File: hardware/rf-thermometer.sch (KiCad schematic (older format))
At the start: 2 parts

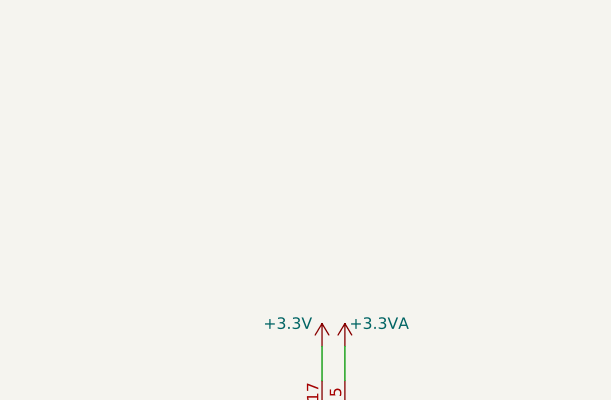
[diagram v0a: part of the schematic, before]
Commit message: Add power bypassing capacitors + filtering inductor for ADC
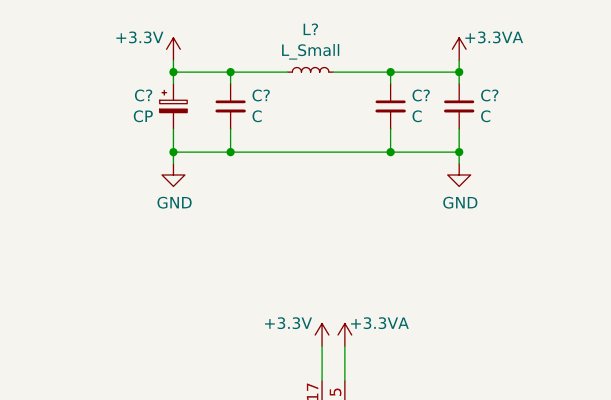
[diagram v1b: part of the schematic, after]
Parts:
- added C?: CP, symbol Device:CP_Small
- added C? (x3): C, symbol Device:C_Small
- added L?: L_Small, symbol Device:L_Small
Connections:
- net +3.3VA: now also C?.1, C?.1, L?.2
- net +3V3: now also C?.1, C?.1, L?.1
- net GND: now also C?.2, C?.2, C?.2, C?.2
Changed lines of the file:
@@
 Wire Wire Line
 	5200 4500 5300 4500
+$Comp
+L Device:CP_Small C?
+U 1 1 5FCC9F0A
+P 5050 1800
+F 0 "C?" H 4962 1846 50  0000 R CNN
+F 1 "CP" H 4962 1755 50  0000 R CNN
+F 2 "" H 5050 1800 50  0001 C CNN
+F 3 "~" H 5050 1800 50  0001 C CNN
+	1    5050 1800
+	1    0    0    -1
+$EndComp
+$Comp
+L Device:C_Small C?
+U 1 1 5FCCA310
+P 5300 1800
+F 0 "C?" H 5392 1846 50  0000 L CNN
+F 1 "C" H 5392 1755 50  0000 L CNN
+F 2 "" H 5300 1800 50  0001 C CNN
+F 3 "~" H 5300 1800 50  0001 C CNN
+	1    5300 1800
+	1    0    0    -1
+$EndComp
+$Comp
+L Device:L_Small L?
+U 1 1 5FCCD1D9
+P 5650 1650
+F 0 "L?" V 5835 1650 50  0000 C CNN
+F 1 "L_Small" V 5744 1650 50  0000 C CNN
+F 2 "" H 5650 1650 50  0001 C CNN
+F 3 "~" H 5650 1650 50  0001 C CNN
+	1    5650 1650
+	0    -1   -1   0
+$EndComp
+$Comp
+L Device:C_Small C?
+U 1 1 5FCCD83A
+P 6000 1800
+F 0 "C?" H 6092 1846 50  0000 L CNN
+F 1 "C" H 6092 1755 50  0000 L CNN
+F 2 "" H 6000 1800 50  0001 C CNN
+F 3 "~" H 6000 1800 50  0001 C CNN
+	1    6000 1800
+	1    0    0    -1
+$EndComp
+$Comp
+L Device:C_Small C?
+U 1 1 5FCCDBEA
+P 6300 1800
+F 0 "C?" H 6392 1846 50  0000 L CNN
+F 1 "C" H 6392 1755 50  0000 L CNN
+F 2 "" H 6300 1800 50  0001 C CNN
+F 3 "~" H 6300 1800 50  0001 C CNN
+	1    6300 1800
+	1    0    0    -1
+$EndComp
+$Comp
+L power:GND #PWR?
+U 1 1 5FCD7767
+P 5050 2050
+F 0 "#PWR?" H 5050 1800 50  0001 C CNN
+F 1 "GND" H 5055 1877 50  0000 C CNN
+F 2 "" H 5050 2050 50  0001 C CNN
+F 3 "" H 5050 2050 50  0001 C CNN
+	1    5050 2050
+	1    0    0    -1
+$EndComp
+$Comp
+L power:GND #PWR?
+U 1 1 5FCD7D7C
+P 6300 2050
+F 0 "#PWR?" H 6300 1800 50  0001 C CNN
+F 1 "GND" H 6305 1877 50  0000 C CNN
+F 2 "" H 6300 2050 50  0001 C CNN
+F 3 "" H 6300 2050 50  0001 C CNN
+	1    6300 2050
+	1    0    0    -1
+$EndComp
+Wire Wire Line
+	5050 1900 5050 2000
+Wire Wire Line
+	5050 2000 5300 2000
+Wire Wire Line
+	6300 2000 6300 1900
+Wire Wire Line
+	6300 2050 6300 2000
+Connection ~ 6300 2000
+Wire Wire Line
+	5050 2050 5050 2000
+Connection ~ 5050 2000
+Wire Wire Line
+	5050 1700 5050 1650
+Wire Wire Line
+	5050 1650 5300 1650
+Wire Wire Line
+	6300 1650 6300 1700
+Wire Wire Line
+	5750 1650 6000 1650
+Wire Wire Line
+	5300 1650 5300 1700
+Wire Wire Line
+	5300 1900 5300 2000
+Connection ~ 5300 1650
+Connection ~ 5300 2000
+Wire Wire Line
+	6000 1650 6000 1700
+Wire Wire Line
+	6000 1900 6000 2000
+Connection ~ 6000 1650
+Wire Wire Line
+	6000 1650 6300 1650
+Connection ~ 6000 2000
+Wire Wire Line
+	6000 2000 6300 2000
+$Comp
+L power:+3.3V #PWR?
+U 1 1 5FCDD47C
+P 5050 1600
+F 0 "#PWR?" H 5050 1450 50  0001 C CNN
+F 1 "+3.3V" H 4900 1700 50  0000 C CNN
+F 2 "" H 5050 1600 50  0001 C CNN
+F 3 "" H 5050 1600 50  0001 C CNN
+	1    5050 1600
+	1    0    0    -1
+$EndComp
+$Comp
+L power:+3.3VA #PWR?
+U 1 1 5FCDD977
+P 6300 1600
+F 0 "#PWR?" H 6300 1450 50  0001 C CNN
+F 1 "+3.3VA" H 6450 1700 50  0000 C CNN
+F 2 "" H 6300 1600 50  0001 C CNN
+F 3 "" H 6300 1600 50  0001 C CNN
+	1    6300 1600
+	1    0    0    -1
+$EndComp
+Wire Wire Line
+	6300 1600 6300 1650
+Connection ~ 6300 1650
+Wire Wire Line
+	5050 1600 5050 1650
+Connection ~ 5050 1650
+Wire Wire Line
+	5300 1650 5550 1650
+Wire Wire Line
+	5300 2000 6000 2000
 $EndSCHEMATC

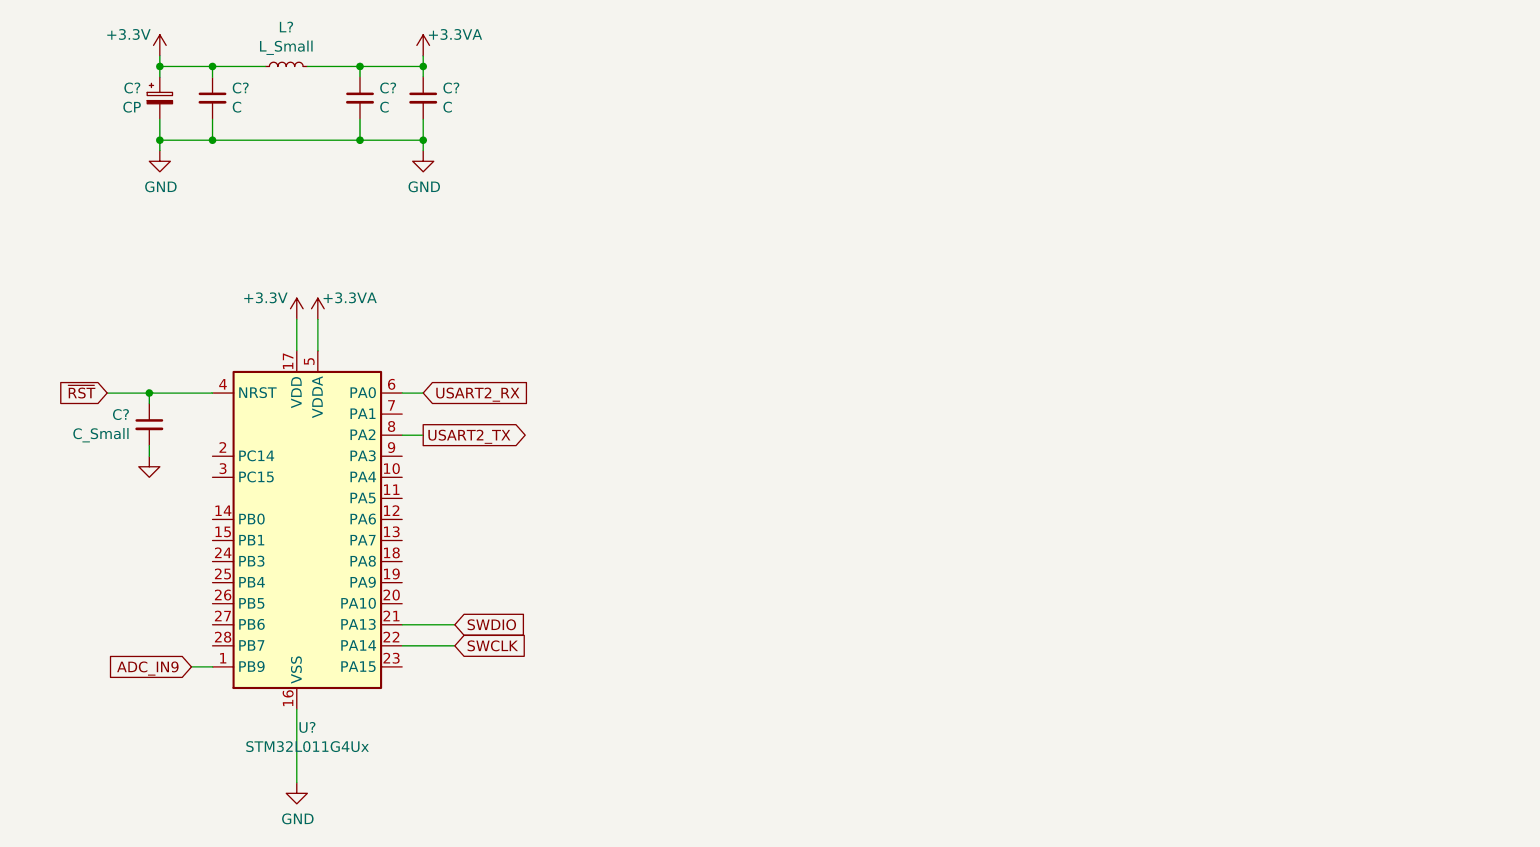
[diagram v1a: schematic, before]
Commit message: NOTATIONAL design based on TDA7100 and Oshpark 4 layer process
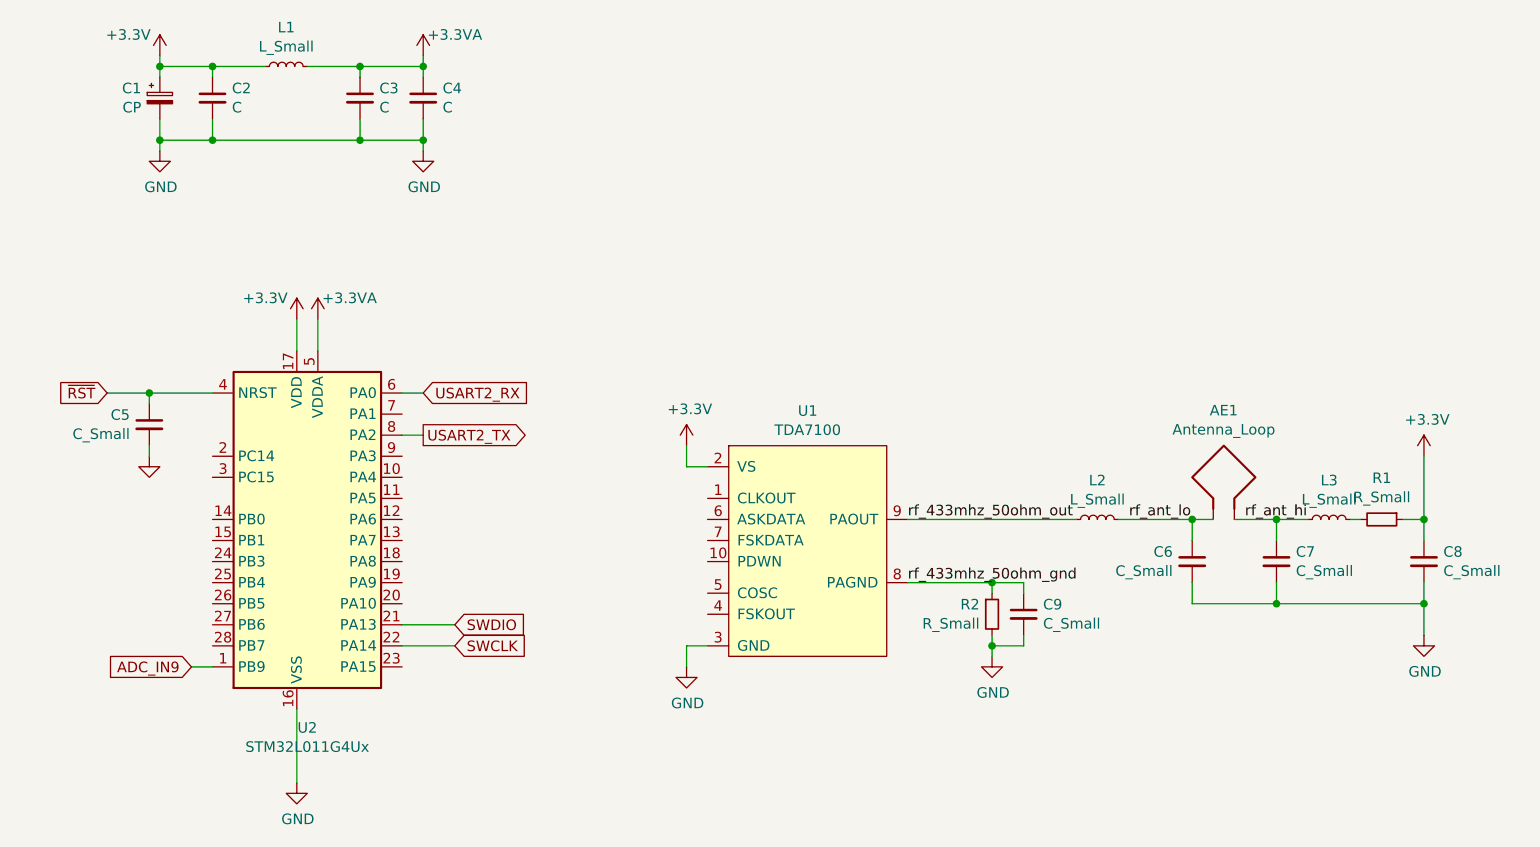
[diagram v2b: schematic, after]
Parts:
- added AE1: Antenna_Loop, RF_Antenna:Coilcraft_MA5532-AE_RFID, symbol Device:Antenna_Loop
- added C6, C7, C8, C9: C_Small, Capacitor_SMD:C_0603_1608Metric, symbol Device:C_Small
- added L2, L3: L_Small, Inductor_SMD:L_0603_1608Metric, symbol Device:L_Small
- added R1, R2: R_Small, Resistor_SMD:R_0603_1608Metric, symbol Device:R_Small
- added U1: TDA7100, Package_SO:TSSOP-10_3x3mm_P0.5mm, symbol rf-tx:TDA7100
- C1: renamed from C?; footprint (none) -> Capacitor_Tantalum_SMD:CP_EIA-3216-18_Kemet-A_Pad1.58x1.35mm_HandSolder
- C2, C3, C4, C5: renamed from C?; footprint (none) -> Capacitor_SMD:C_0805_2012Metric
- L1: renamed from L?; footprint (none) -> Inductor_SMD:L_0603_1608Metric
- gave numbers to parts that had none: 1
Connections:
- net +3V3: now also C8.1, R1.1, U1.2 (VS)
- net GND: now also C6.2, C7.2, C8.2, C9.2, R2.2, U1.3 (GND)
- new net: L3.2, R1.2
- new net rf_433mhz_50ohm_gnd: C9.1, R2.1, U1.8 (PAGND)
- new net rf_433mhz_50ohm_out: L2.1, U1.9 (PAOUT)
- new net rf_ant_hi: AE1.2, C7.1, L3.1
- new net rf_ant_lo: AE1.1, C6.1, L2.2
